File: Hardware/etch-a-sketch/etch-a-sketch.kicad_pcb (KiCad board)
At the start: 4 copper layers, 100 x 62 mm, 37 parts, among them J1 USART, J2 Conn_02x05_Odd_Even, J3 OLED, J4 Power Connector, SW1 Encoder 1, SW2 Encoder 2, U1 AMS1117-3.3, U2 STM32F401RET6

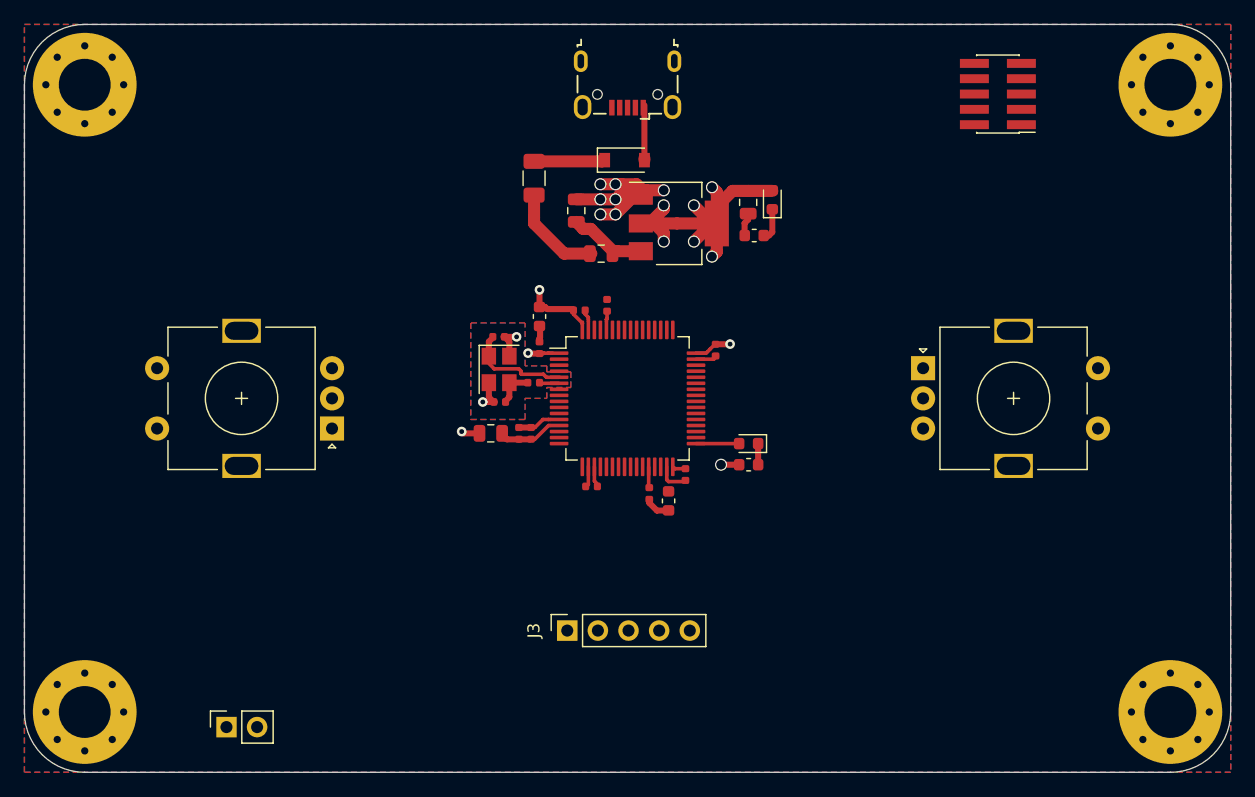
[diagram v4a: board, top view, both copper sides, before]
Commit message: feat: complete initial routing
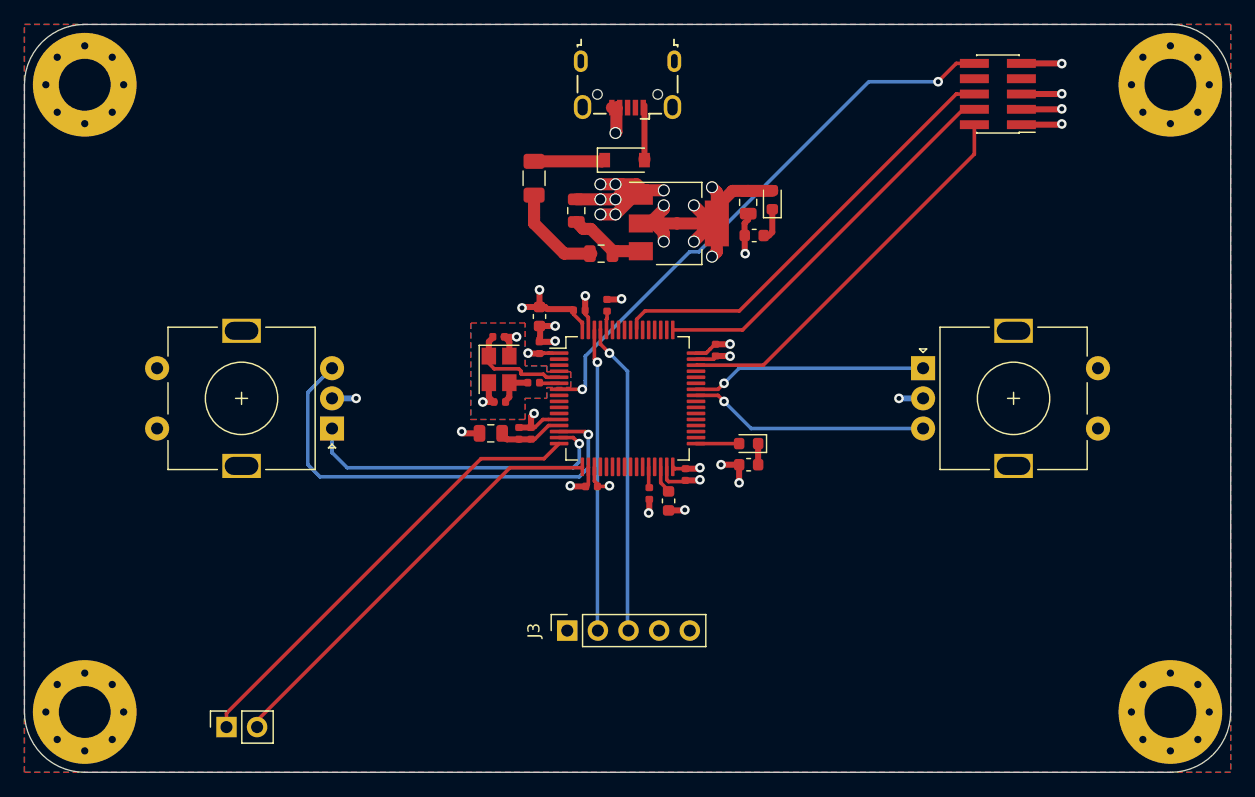
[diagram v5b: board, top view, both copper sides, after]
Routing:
- net NRST: track 0.00 -> 47.4 mm, vias 0 -> 2
- net ENC2_B: track 0.00 -> 38.1 mm, vias 0 -> 1
- net USART2_TX: track 0.00 -> 38.0 mm
- net SWO: track 0.00 -> 36.5 mm
- net USART2_RX: track 0.00 -> 36.3 mm
- net SWCLK: track 0.00 -> 32.6 mm
- net SWDIO: track 0.00 -> 32.6 mm
- net GND: track 40.1 -> 71.2 mm, vias 10 -> 28
- net ENC2_A: track 0.00 -> 26.6 mm, vias 0 -> 1
- net OLED_SCL: track 0.00 -> 25.7 mm, vias 0 -> 1
- net OLED_SDA: track 0.00 -> 25.0 mm, vias 0 -> 1
- net ENC1_B: track 0.00 -> 20.0 mm, vias 0 -> 1
- net ENC1_A: track 0.00 -> 19.5 mm, vias 0 -> 1
- net +3V3: track 46.5 -> 53.6 mm, vias 10 -> 14
- net Net-(C11-Pad1): track 0.00 -> 2.39 mm

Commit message: feat: add silkscreen labels
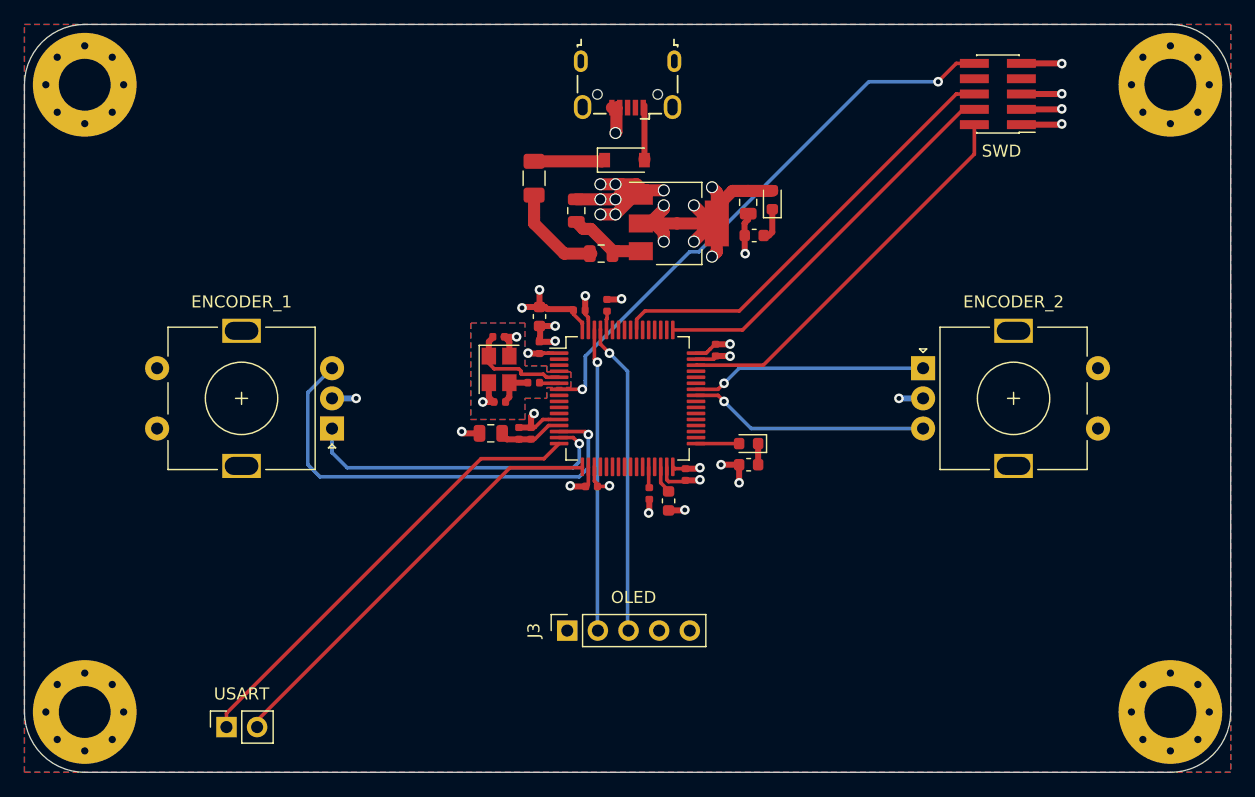
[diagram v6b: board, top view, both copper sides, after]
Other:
- board text added: "ENCODER_1"
- board text added: "ENCODER_2"
- board text added: "OLED"
- board text added: "SWD"
- board text added: "USART"
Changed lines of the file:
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@@
   (general
     (thickness 1.6)
-    (drawings 8)
+    (drawings 13)
     (tracks 309)
     (zones 0)
@@
     )
   )
+  (gr_text SWD (at 101 30.5) (layer F.SilkS)
+    (effects (font (size 1 1) (thickness 0.15)))
+  )
+  (gr_text USART (at 38 75.5) (layer F.SilkS)
+    (effects (font (size 1 1) (thickness 0.15)))
+  )
+  (gr_text ENCODER_2 (at 102 43) (layer F.SilkS)
+    (effects (font (size 1 1) (thickness 0.15)))
+  )
+  (gr_text ENCODER_1 (at 38 43) (layer F.SilkS)
+    (effects (font (size 1 1) (thickness 0.15)))
+  )
+  (gr_text OLED (at 70.5 67.5) (layer F.SilkS)
+    (effects (font (size 1 1) (thickness 0.15)))
+  )
   (gr_arc (start 115 77) (end 115 82) (angle -90) (layer Edge.Cuts) (width 0.05))

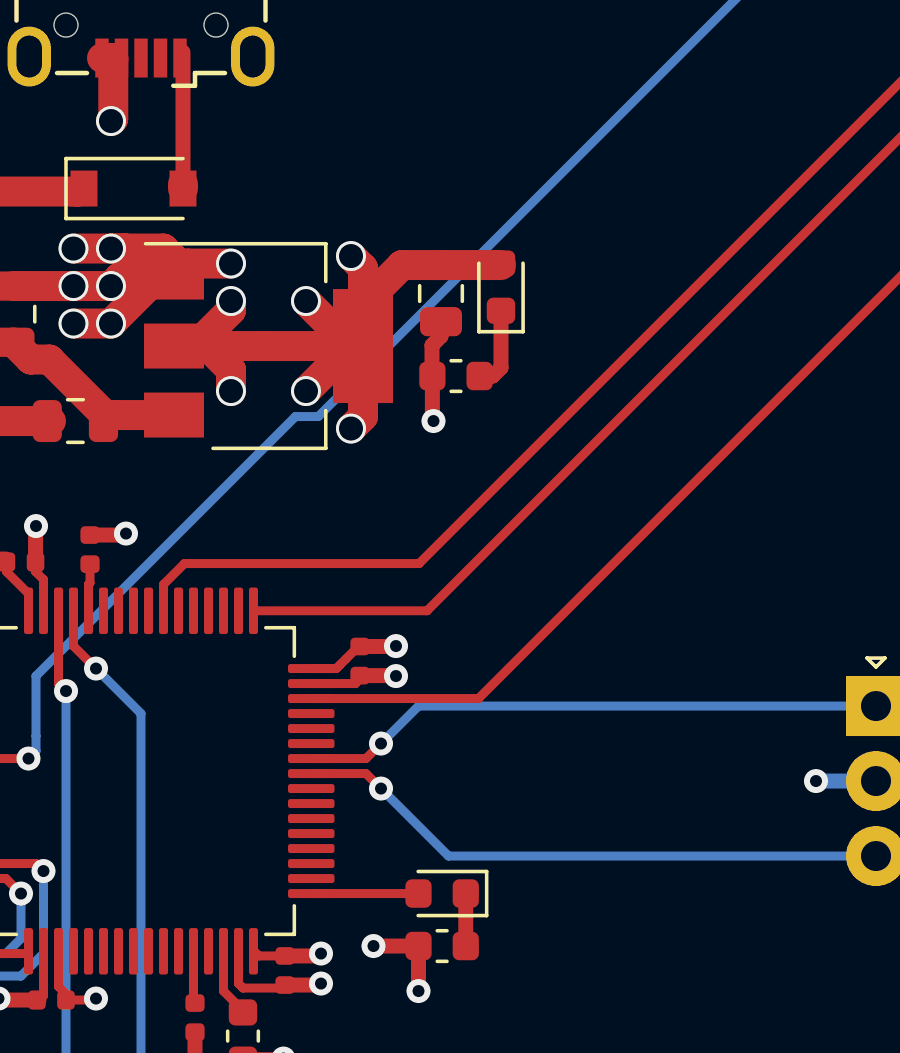
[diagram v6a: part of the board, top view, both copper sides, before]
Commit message: feat: add labels for power, status LED, and connectors
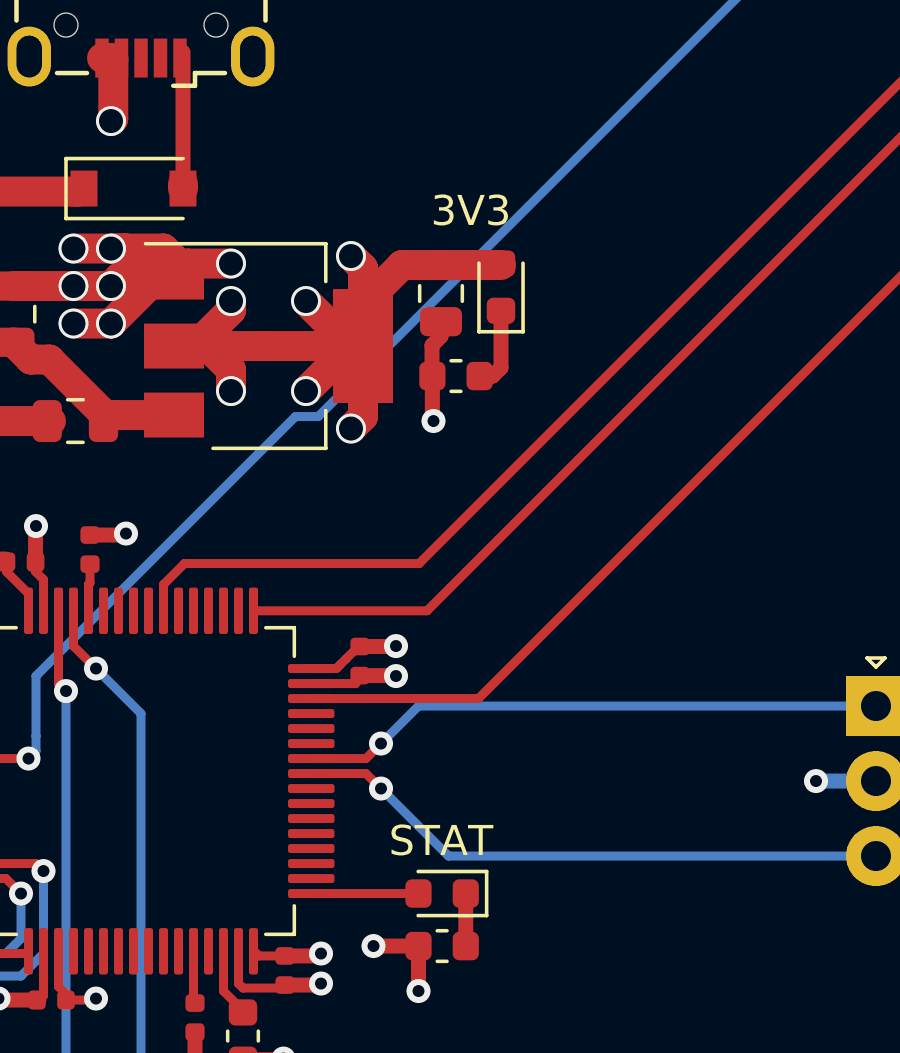
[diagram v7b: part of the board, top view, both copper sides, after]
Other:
- board text added: "3V3"
- board text added: "GND"
- board text added: "RX"
- board text added: "SCL"
- board text added: "SDA"
- board text added: "STAT"
- board text added: "TX"
- board text added: "X"
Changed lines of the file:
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@@
   (general
     (thickness 1.6)
-    (drawings 13)
+    (drawings 22)
     (tracks 309)
     (zones 0)
@@
     (33 F.Adhes user)
     (35 F.Paste user)
+    (36 B.SilkS user)
     (37 F.SilkS user)
     (39 F.Mask user)
@@
     )
   )
+  (gr_text STAT (at 80 53) (layer F.SilkS)
+    (effects (font (size 1 1) (thickness 0.15)))
+  )
+  (gr_text 3V3 (at 81 32) (layer F.SilkS)
+    (effects (font (size 1 1) (thickness 0.15)))
+  )
+  (gr_text GND (at 75.25 73.75 90) (layer B.SilkS)
+    (effects (font (size 1 1) (thickness 0.15)) (justify mirror))
+  )
+  (gr_text X (at 72.75 73.75 90) (layer B.SilkS)
+    (effects (font (size 1 1) (thickness 0.15)) (justify mirror))
+  )
+  (gr_text SCL (at 70.25 73.75 90) (layer B.SilkS)
+    (effects (font (size 1 1) (thickness 0.15)) (justify mirror))
+  )
+  (gr_text SDA (at 67.75 73.75 90) (layer B.SilkS)
+    (effects (font (size 1 1) (thickness 0.15)) (justify mirror))
+  )
+  (gr_text 3V3 (at 65 73.75 90) (layer B.SilkS)
+    (effects (font (size 1 1) (thickness 0.15)) (justify mirror))
+  )
+  (gr_text RX (at 39.25 75.25 90) (layer B.SilkS)
+    (effects (font (size 1 1) (thickness 0.15)) (justify mirror))
+  )
+  (gr_text TX (at 36.75 75.25 90) (layer B.SilkS)
+    (effects (font (size 1 1) (thickness 0.15)) (justify mirror))
+  )
   (gr_text SWD (at 101 30.5) (layer F.SilkS)

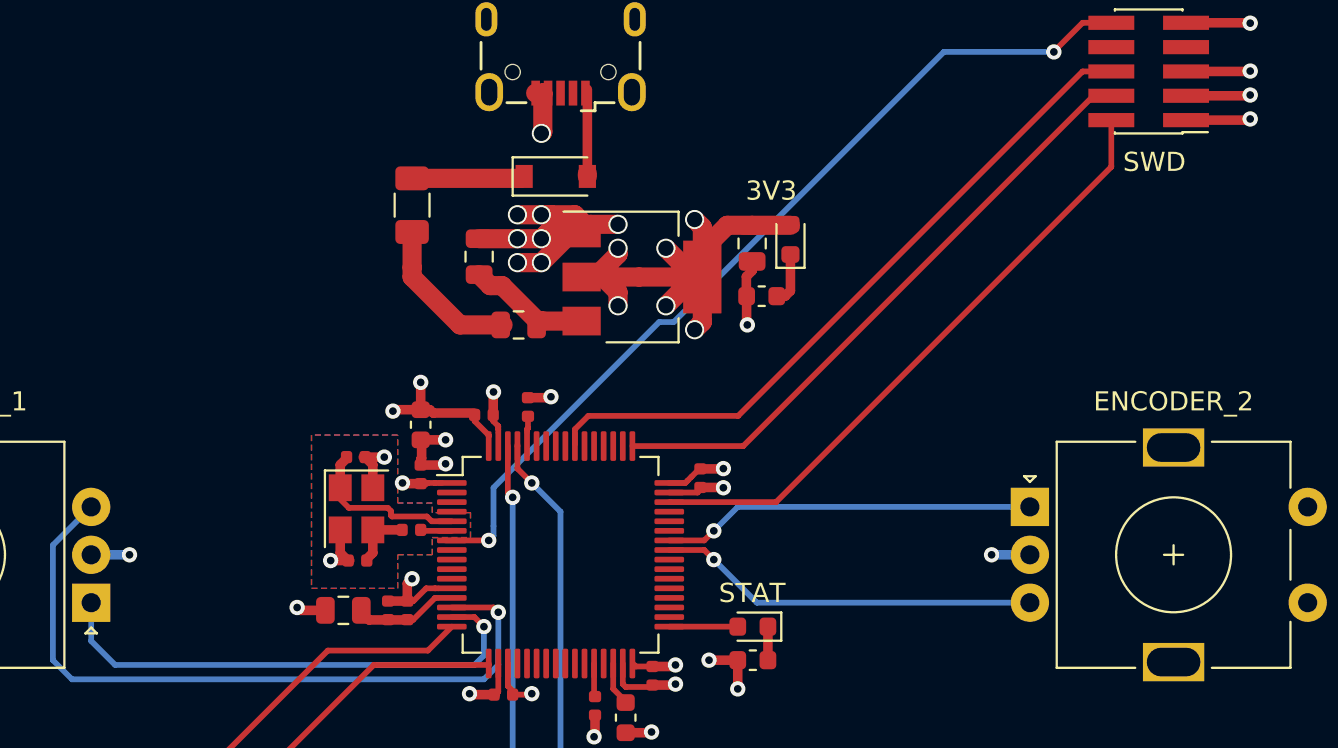
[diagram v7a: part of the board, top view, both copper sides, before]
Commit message: feat: add polarity and pin 1 markers
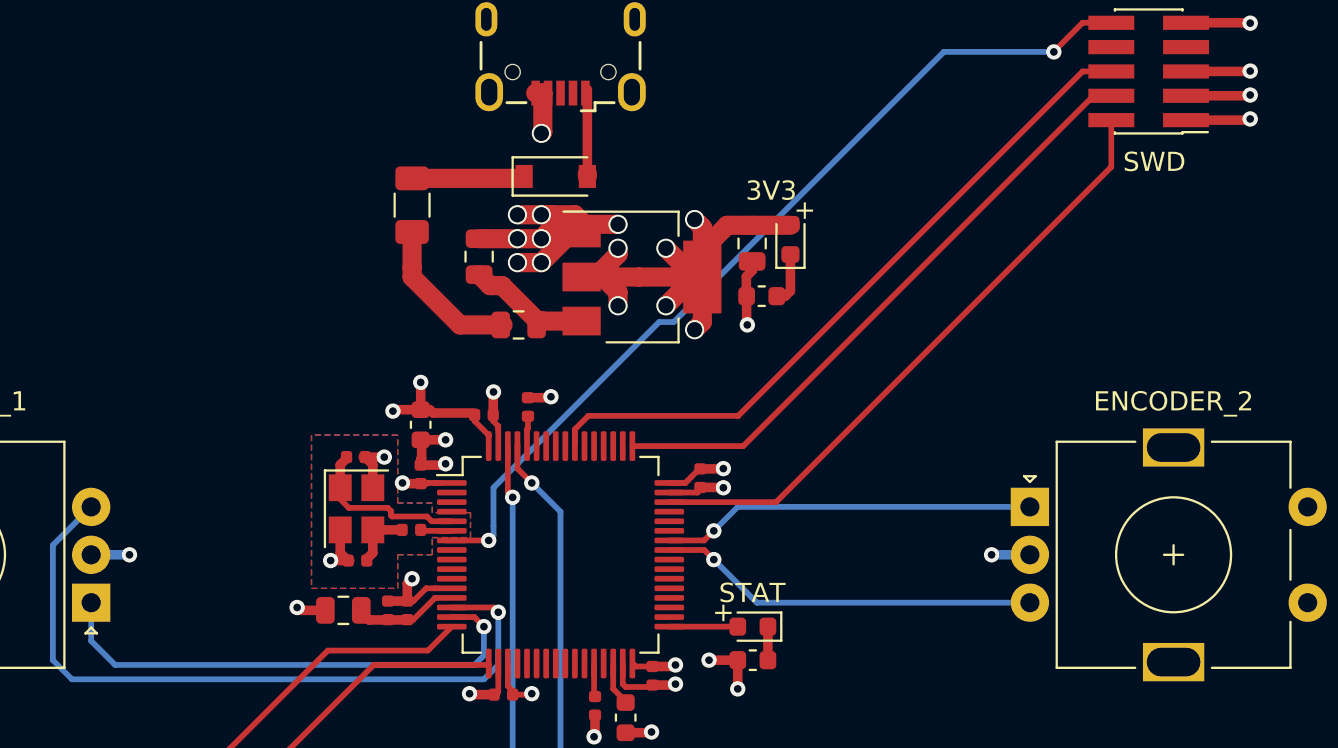
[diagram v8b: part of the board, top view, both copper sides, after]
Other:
- board text added: "+"
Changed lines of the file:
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@@
   (general
     (thickness 1.6)
-    (drawings 22)
+    (drawings 30)
     (tracks 309)
     (zones 0)
@@
     )
   )
+  (gr_circle (center 46.8 53.5) (end 46.8 53.5) (layer F.SilkS) (width 0.12))
+  (gr_circle (center 93.2 48.5) (end 93.2 48.5) (layer F.SilkS) (width 0.12))
+  (gr_circle (center 71.4 28.1) (end 71.4 28.1) (layer F.SilkS) (width 0.12))
+  (gr_circle (center 104.5 28.3) (end 104.5 28.3) (layer F.SilkS) (width 0.12))
+  (gr_circle (center 58.5 46.4) (end 58.5 46.4) (layer F.SilkS) (width 0.12))
+  (gr_circle (center 63.3 47.25) (end 63.3 47.25) (layer F.SilkS) (width 0.12))
+  (gr_text + (at 82.75 33) (layer F.SilkS)
+    (effects (font (size 1 1) (thickness 0.15)))
+  )
+  (gr_text + (at 78.5 54) (layer F.SilkS)
+    (effects (font (size 1 1) (thickness 0.15)))
+  )
   (gr_text STAT (at 80 53) (layer F.SilkS)
